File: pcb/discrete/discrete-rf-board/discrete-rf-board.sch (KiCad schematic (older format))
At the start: 8 parts, among them J101 Conn_Coaxial, U101 BGS12PL6E6327XTSA1, U102 BGS12PL6E6327XTSA1

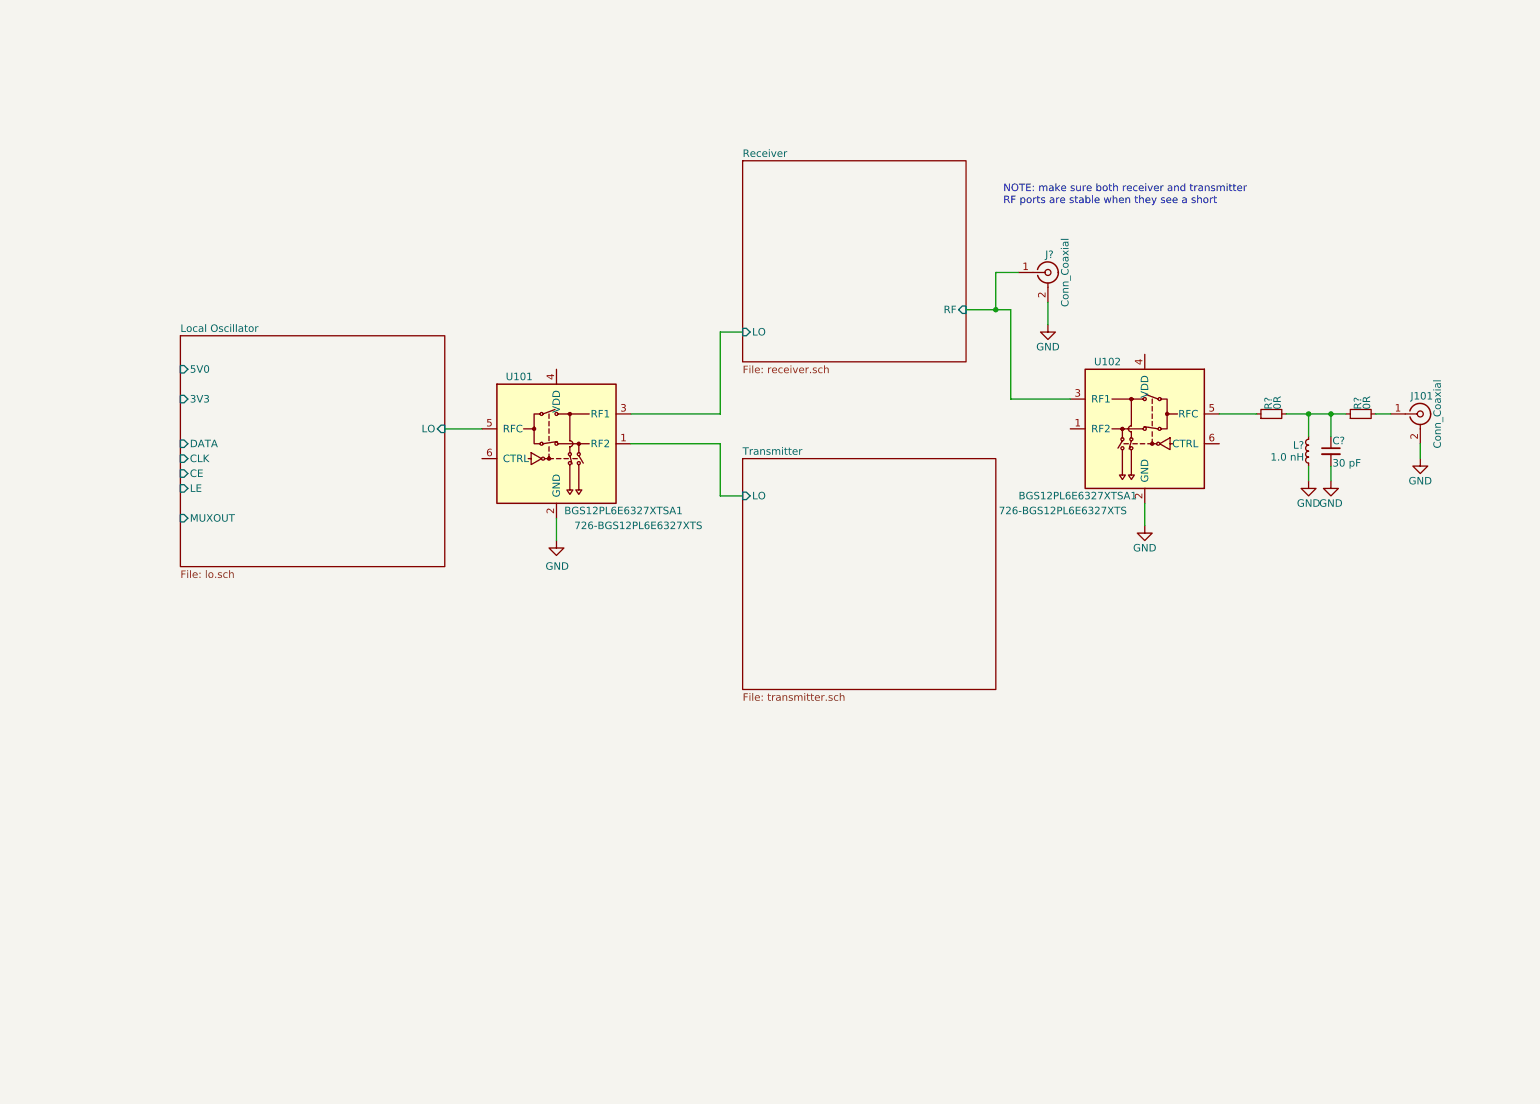
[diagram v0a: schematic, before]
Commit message: Design DAC/ADC stages, pass out all control signals to top sheet
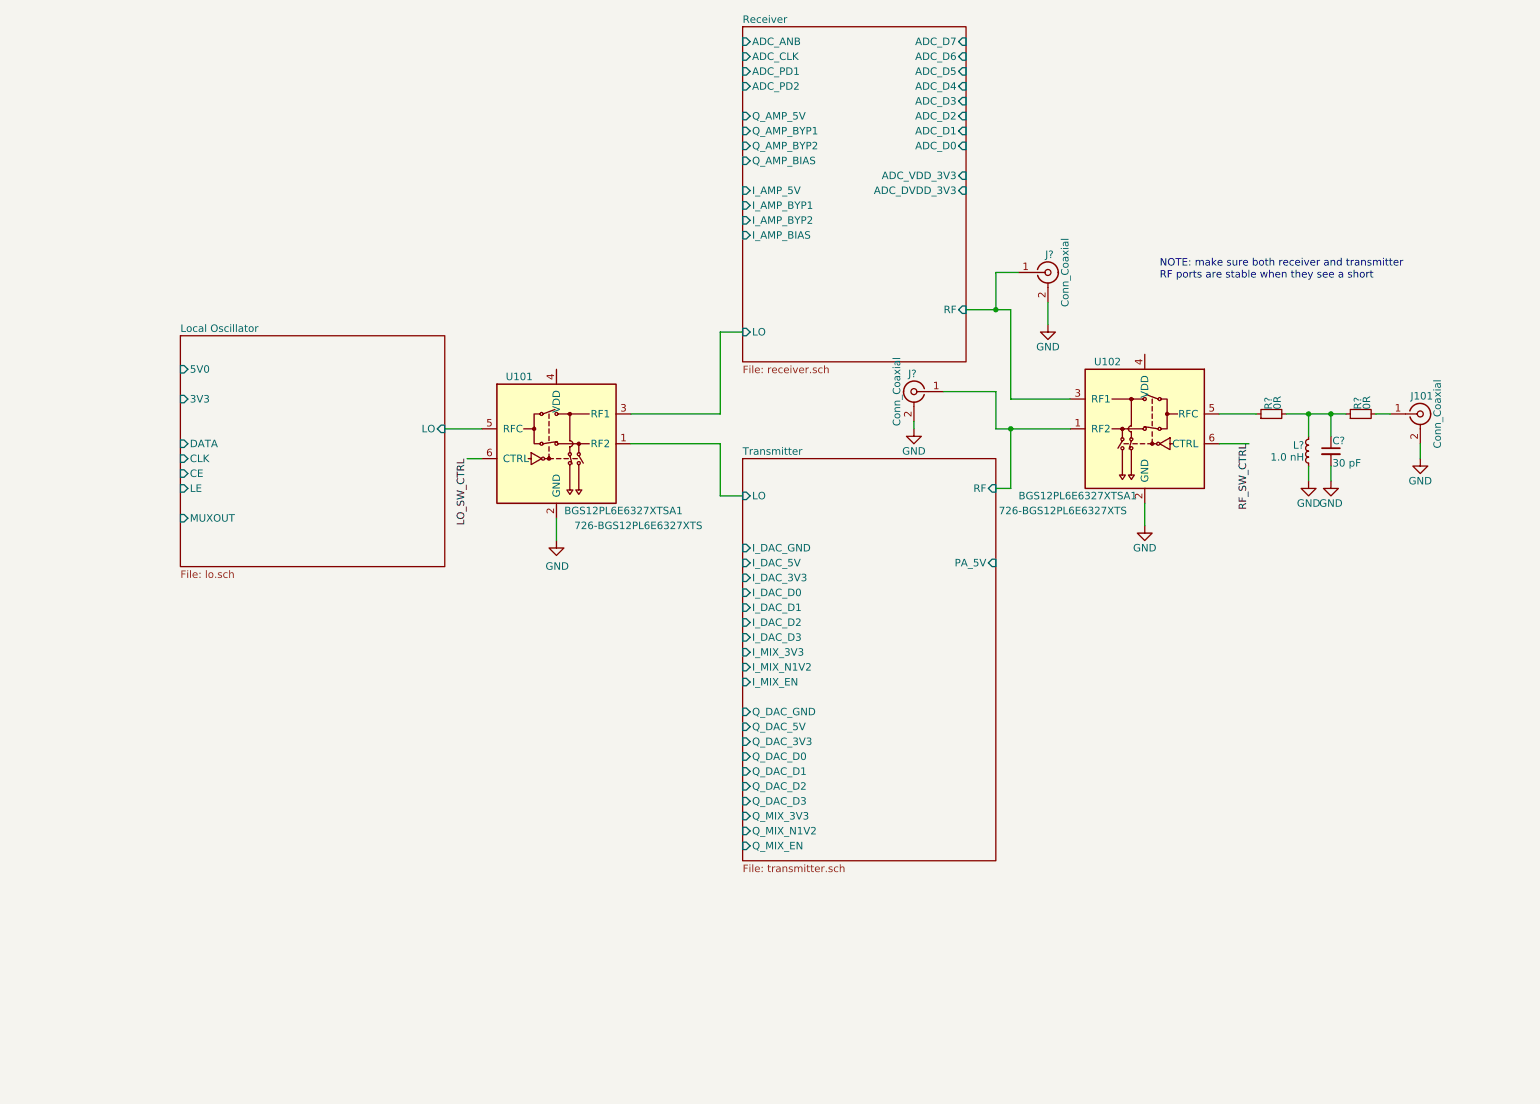
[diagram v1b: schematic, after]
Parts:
- added J?: Conn_Coaxial, symbol Connector:Conn_Coaxial
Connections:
- net GND: now also J?.2 (Ext)
- net LO_SW_CTRL: now reaches U101.6 (CTRL)
- net Transmitter/RF: now reaches U102.1 (RF2)
- net Transmitter/RF: now also J?.1 (In)
- net RF_SW_CTRL: now reaches U102.6 (CTRL)
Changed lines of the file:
@@
 $EndDescr
 $Sheet
-S 5600 1550 1500 1350
-U 5CA6B0AA
-F0 "Receiver" 50
-F1 "receiver.sch" 50
-F2 "RF" I R 7100 2550 50
-F3 "LO" I L 5600 2700 50
-$EndSheet
-$Sheet
-S 5600 3550 1700 1550
+S 5600 3550 1700 2700
 U 5CA6B0B3
 F0 "Transmitter" 50
 F1 "transmitter.sch" 50
 F2 "LO" I L 5600 3800 50
+F3 "RF" I R 7300 3750 50
+F4 "I_DAC_D0" I L 5600 4450 50
+F5 "I_DAC_D1" I L 5600 4550 50
+F6 "I_DAC_D2" I L 5600 4650 50
+F7 "I_DAC_D3" I L 5600 4750 50
+F8 "I_DAC_3V3" I L 5600 4350 50
+F9 "I_DAC_5V" I L 5600 4250 50
+F10 "I_MIX_EN" I L 5600 5050 50
+F11 "I_MIX_3V3" I L 5600 4850 50
+F12 "I_MIX_N1V2" I L 5600 4950 50
+F13 "Q_MIX_3V3" I L 5600 5950 50
+F14 "Q_MIX_N1V2" I L 5600 6050 50
+F15 "Q_MIX_EN" I L 5600 6150 50
+F16 "PA_5V" I R 7300 4250 50
+F17 "Q_DAC_5V" I L 5600 5350 50
+F18 "Q_DAC_3V3" I L 5600 5450 50
+F19 "Q_DAC_D0" I L 5600 5550 50
+F20 "Q_DAC_D1" I L 5600 5650 50
+F21 "Q_DAC_D2" I L 5600 5750 50
+F22 "Q_DAC_D3" I L 5600 5850 50
+F23 "I_DAC_GND" I L 5600 4150 50
+F24 "Q_DAC_GND" I L 5600 5250 50
 $EndSheet
 $Comp
@@
 Wire Wire Line
 	9550 3700 9550 3600
-Text Notes 7350 1850 0    50   ~ 0
+Text Notes 8400 2350 0    50   ~ 0
 NOTE: make sure both receiver and transmitter\nRF ports are stable when they see a short
 $Comp
@@
 Wire Wire Line
 	5450 2700 5600 2700
+Wire Wire Line
+	7400 3750 7400 3350
+Wire Wire Line
+	7400 3350 7800 3350
+Wire Wire Line
+	7300 3750 7400 3750
+$Comp
+L Connector:Conn_Coaxial J?
+U 1 1 5D983CB7
+P 6750 3100
+F 0 "J?" H 6760 3220 50  0000 C CNN
+F 1 "Conn_Coaxial" V 6865 3100 50  0000 C CNN
+F 2 "" H 6750 3100 50  0001 C CNN
+F 3 " ~" H 6750 3100 50  0001 C CNN
+	1    6750 3100
+	-1   0    0    -1
+$EndComp
+Wire Wire Line
+	6950 3100 7300 3100
+Wire Wire Line
+	7300 3100 7300 3350
+Wire Wire Line
+	7300 3350 7400 3350
+Connection ~ 7400 3350
+$Comp
+L power:GND #PWR?
+U 1 1 5D989BE4
+P 6750 3350
+F 0 "#PWR?" H 6750 3100 50  0001 C CNN
+F 1 "GND" H 6750 3200 50  0000 C CNN
+F 2 "" H 6750 3350 50  0001 C CNN
+F 3 "" H 6750 3350 50  0001 C CNN
+	1    6750 3350
+	1    0    0    -1
+$EndComp
+Wire Wire Line
+	6750 3350 6750 3300
+$Sheet
+S 5600 650  1500 2250
+U 5CA6B0AA
+F0 "Receiver" 50
+F1 "receiver.sch" 50
+F2 "RF" I R 7100 2550 50
+F3 "LO" I L 5600 2700 50
+F4 "ADC_ANB" I L 5600 750 50
+F5 "ADC_CLK" I L 5600 850 50
+F6 "ADC_PD1" I L 5600 950 50
+F7 "ADC_PD2" I L 5600 1050 50
+F8 "ADC_D7" I R 7100 750 50
+F9 "ADC_D6" I R 7100 850 50
+F10 "ADC_D5" I R 7100 950 50
+F11 "ADC_D4" I R 7100 1050 50
+F12 "ADC_D3" I R 7100 1150 50
+F13 "ADC_D2" I R 7100 1250 50
+F14 "ADC_D1" I R 7100 1350 50
+F15 "ADC_D0" I R 7100 1450 50
+F16 "Q_AMP_5V" I L 5600 1250 50
+F17 "Q_AMP_BYP1" I L 5600 1350 50
+F18 "Q_AMP_BYP2" I L 5600 1450 50
+F19 "Q_AMP_BIAS" I L 5600 1550 50
+F20 "ADC_VDD_3V3" I R 7100 1650 50
+F21 "ADC_DVDD_3V3" I R 7100 1750 50
+F22 "I_AMP_5V" I L 5600 1750 50
+F23 "I_AMP_BYP1" I L 5600 1850 50
+F24 "I_AMP_BYP2" I L 5600 1950 50
+F25 "I_AMP_BIAS" I L 5600 2050 50
+$EndSheet
+Text Label 3750 3550 3    50   ~ 0
+LO_SW_CTRL
+Wire Wire Line
+	3750 3550 3850 3550
+Text Label 9000 3450 3    50   ~ 0
+RF_SW_CTRL
+Wire Wire Line
+	9000 3450 8800 3450
 $EndSCHEMATC

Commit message: Wire out all control signals to connectors TODO PLL charge pump loop, bypass caps in attenuator circuit, antialiasing filter for ADC frontend
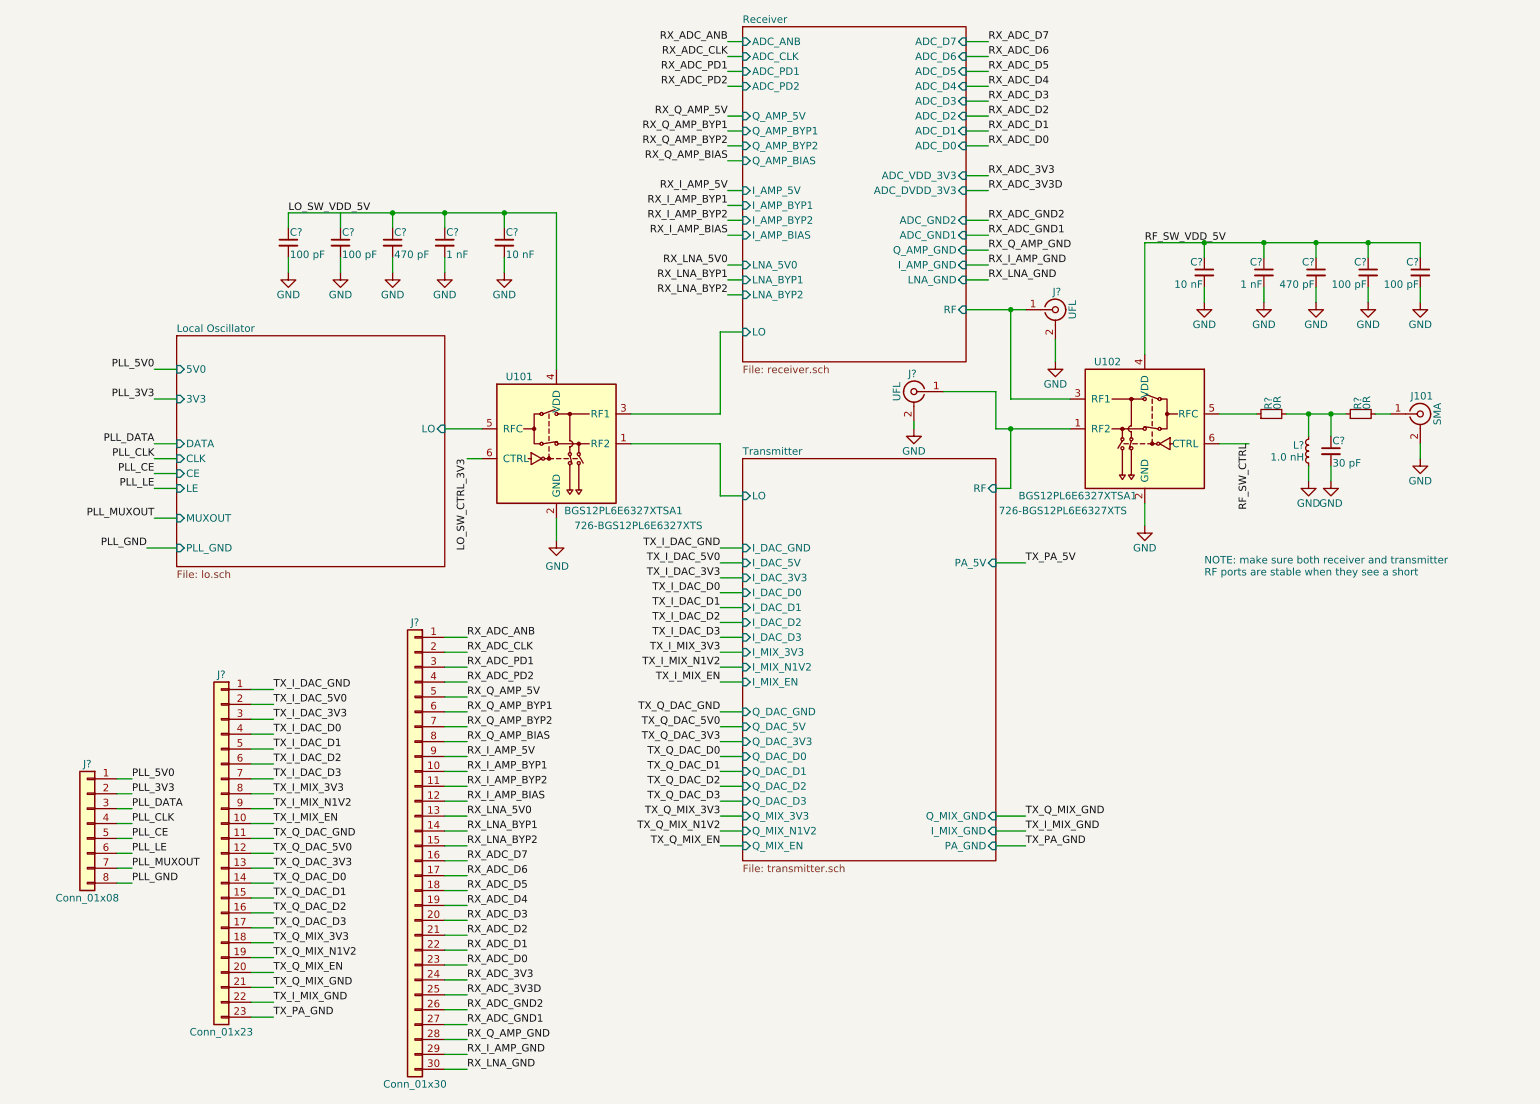
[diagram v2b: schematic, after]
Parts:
- added C? (x2): 1 nF, symbol Device:C_Small
- added C? (x2): 10 nF, symbol Device:C_Small
- added C? (x2): 470 pF, symbol Device:C_Small
- added C? (x4): 100 pF, symbol Device:C_Small
- added J?: Conn_01x08, symbol Connector_Generic:Conn_01x08
- added J?: Conn_01x23, symbol Connector_Generic:Conn_01x23
- added J?: Conn_01x30, symbol Connector_Generic:Conn_01x30
- J101: value Conn_Coaxial -> SMA
- J? (x2): value Conn_Coaxial -> UFL
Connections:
- net GND: now also C?.2, C?.2, C?.2, C?.2, C?.2, C?.2, C?.2, C?.2, C?.2, C?.2
- net LO_SW_VDD_5V: now reaches U101.4 (VDD)
- net LO_SW_VDD_5V: now also C?.1, C?.1, C?.1, C?.1, C?.1
- net RF_SW_VDD_5V: now reaches U102.4 (VDD)
- net RF_SW_VDD_5V: now also C?.1, C?.1, C?.1, C?.1, C?.1
- net LO_SW_CTRL renamed LO_SW_CTRL_3V3
- new net PLL_3V3: J?.2 (Pin_2)
- new net PLL_5V0: J?.1 (Pin_1)
- new net PLL_CE: J?.5 (Pin_5)
- new net PLL_CLK: J?.4 (Pin_4)
- new net PLL_DATA: J?.3 (Pin_3)
- new net PLL_GND: J?.8 (Pin_8)
- new net PLL_LE: J?.6 (Pin_6)
- new net PLL_MUXOUT: J?.7 (Pin_7)
- new net RX_ADC_3V3: J?.24 (Pin_24)
- new net RX_ADC_3V3D: J?.25 (Pin_25)
- new net RX_ADC_ANB: J?.1 (Pin_1)
- new net RX_ADC_CLK: J?.2 (Pin_2)
- new net RX_ADC_D0: J?.23 (Pin_23)
- new net RX_ADC_D1: J?.22 (Pin_22)
- new net RX_ADC_D2: J?.21 (Pin_21)
- new net RX_ADC_D3: J?.20 (Pin_20)
- new net RX_ADC_D4: J?.19 (Pin_19)
- new net RX_ADC_D5: J?.18 (Pin_18)
- new net RX_ADC_D6: J?.17 (Pin_17)
- new net RX_ADC_D7: J?.16 (Pin_16)
- new net RX_ADC_GND1: J?.27 (Pin_27)
- new net RX_ADC_GND2: J?.26 (Pin_26)
- new net RX_ADC_PD1: J?.3 (Pin_3)
- new net RX_ADC_PD2: J?.4 (Pin_4)
- new net RX_I_AMP_5V: J?.9 (Pin_9)
- new net RX_I_AMP_BIAS: J?.12 (Pin_12)
- new net RX_I_AMP_BYP1: J?.10 (Pin_10)
- new net RX_I_AMP_BYP2: J?.11 (Pin_11)
- new net RX_I_AMP_GND: J?.29 (Pin_29)
- new net RX_LNA_5V0: J?.13 (Pin_13)
- new net RX_LNA_BYP1: J?.14 (Pin_14)
- new net RX_LNA_BYP2: J?.15 (Pin_15)
- new net RX_LNA_GND: J?.30 (Pin_30)
- new net RX_Q_AMP_5V: J?.5 (Pin_5)
- new net RX_Q_AMP_BIAS: J?.8 (Pin_8)
- new net RX_Q_AMP_BYP1: J?.6 (Pin_6)
- new net RX_Q_AMP_BYP2: J?.7 (Pin_7)
- new net RX_Q_AMP_GND: J?.28 (Pin_28)
- new net TX_I_DAC_3V3: J?.3 (Pin_3)
- new net TX_I_DAC_5V0: J?.2 (Pin_2)
- new net TX_I_DAC_D0: J?.4 (Pin_4)
- new net TX_I_DAC_D1: J?.5 (Pin_5)
- new net TX_I_DAC_D2: J?.6 (Pin_6)
- new net TX_I_DAC_D3: J?.7 (Pin_7)
- new net TX_I_DAC_GND: J?.1 (Pin_1)
- new net TX_I_MIX_3V3: J?.8 (Pin_8)
- new net TX_I_MIX_EN: J?.10 (Pin_10)
- new net TX_I_MIX_GND: J?.22 (Pin_22)
- new net TX_I_MIX_N1V2: J?.9 (Pin_9)
- new net TX_PA_GND: J?.23 (Pin_23)
- new net TX_Q_DAC_3V3: J?.13 (Pin_13)
- new net TX_Q_DAC_5V0: J?.12 (Pin_12)
- new net TX_Q_DAC_D0: J?.14 (Pin_14)
- new net TX_Q_DAC_D1: J?.15 (Pin_15)
- new net TX_Q_DAC_D2: J?.16 (Pin_16)
- new net TX_Q_DAC_D3: J?.17 (Pin_17)
- new net TX_Q_DAC_GND: J?.11 (Pin_11)
- new net TX_Q_MIX_3V3: J?.18 (Pin_18)
- new net TX_Q_MIX_EN: J?.20 (Pin_20)
- new net TX_Q_MIX_GND: J?.21 (Pin_21)
- new net TX_Q_MIX_N1V2: J?.19 (Pin_19)
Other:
- moved on the sheet: J?
